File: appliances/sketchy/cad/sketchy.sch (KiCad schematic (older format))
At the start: 6 parts, among them J1 Barrel_Jack, M1 Stepper_Motor_bipolar, M2 Stepper_Motor_bipolar, U1 ESP32PICO-KIT

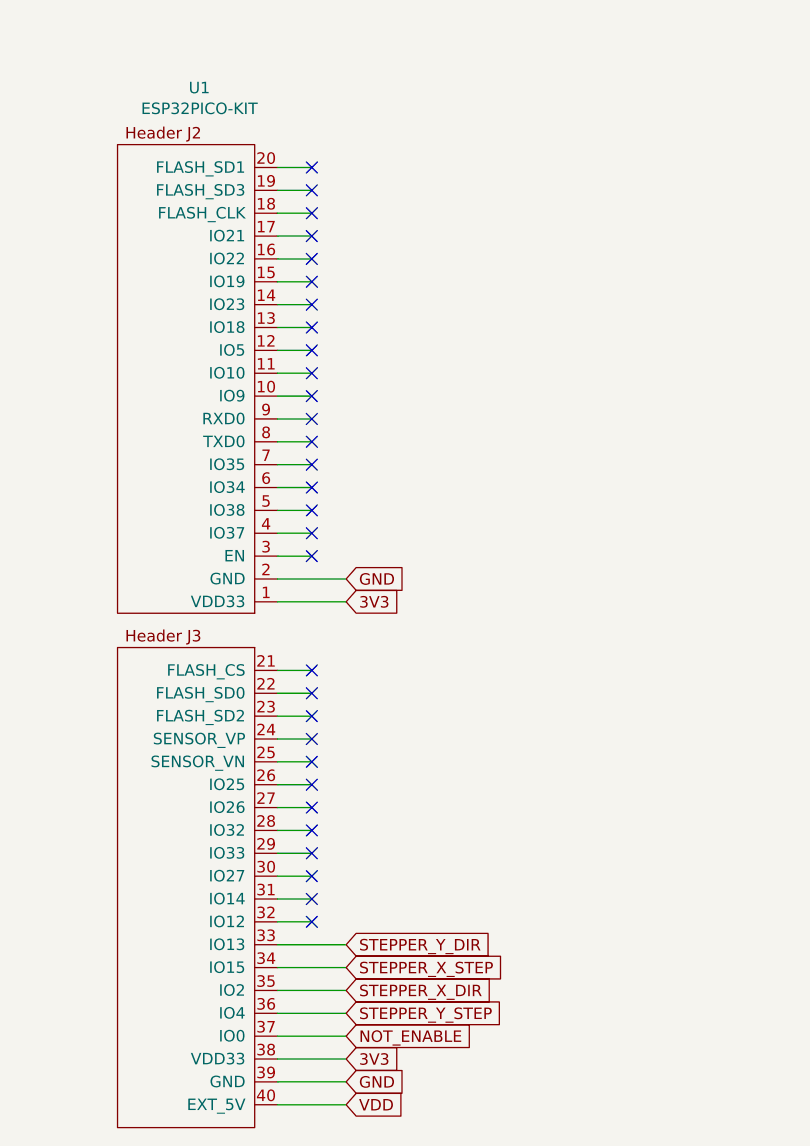
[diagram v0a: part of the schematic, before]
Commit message: Created smaller, square PCB with easy access to ESP32-PICO-KIT USB port.
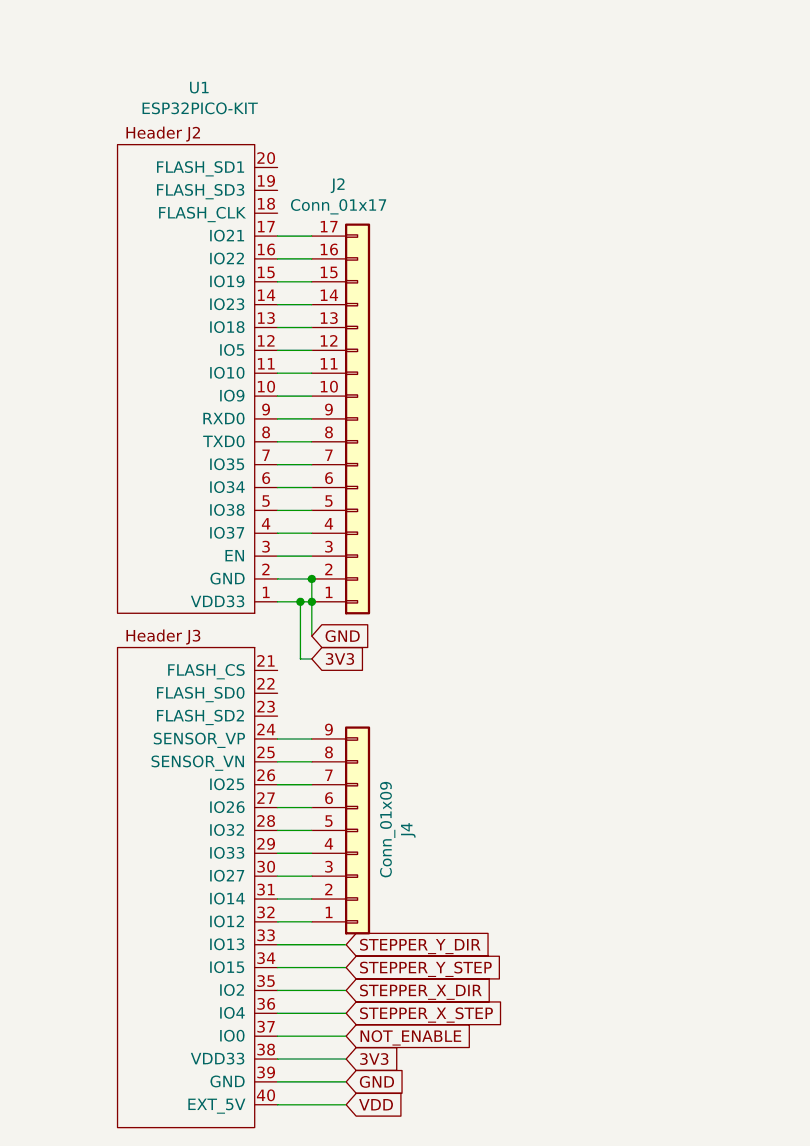
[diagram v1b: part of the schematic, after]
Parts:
- added J2: Conn_01x17, symbol Connector_Generic:Conn_01x17
- added J4: Conn_01x09, Pin_Header_Straight_1x09_Pitch2.54mm, symbol Connector_Generic:Conn_01x09
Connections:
- net GND is gone; now on net 3V3: A1.1 (GND), A1.10 (MS1), A1.11 (MS2), A1.12 (MS3), A1.7 (GND), A2.1 (GND), A2.10 (MS1), A2.11 (MS2), A2.12 (MS3), A2.7 (GND), J1.2, U1.2 (GND), U1.39 (GND)
- net 3V3: now also J2.1 (Pin_1), J2.2 (Pin_2)
- net STEPPER_X_STEP: now also U1.36 (IO4); no longer U1.34 (IO15)
- net STEPPER_Y_STEP: now also U1.34 (IO15); no longer U1.36 (IO4)
- net at U1.10 (IO9): now also J2.10 (Pin_10)
- net at U1.11 (IO10): now also J2.11 (Pin_11)
- net at U1.12 (IO5): now also J2.12 (Pin_12)
- net at U1.13 (IO18): now also J2.13 (Pin_13)
- net at U1.14 (IO23): now also J2.14 (Pin_14)
- net at U1.15 (IO19): now also J2.15 (Pin_15)
- net at U1.16 (IO22): now also J2.16 (Pin_16)
- net at U1.17 (IO21): now also J2.17 (Pin_17)
- net at U1.24 (SENSOR_VP): now also J4.9 (Pin_9)
- net at U1.25 (SENSOR_VN): now also J4.8 (Pin_8)
- net at U1.26 (IO25): now also J4.7 (Pin_7)
- net at U1.27 (IO26): now also J4.6 (Pin_6)
- net at U1.28 (IO32): now also J4.5 (Pin_5)
- net at U1.29 (IO33): now also J4.4 (Pin_4)
- net at U1.3 (EN): now also J2.3 (Pin_3)
- net at U1.30 (IO27): now also J4.3 (Pin_3)
- net at U1.31 (IO14): now also J4.2 (Pin_2)
- net at U1.32 (IO12): now also J4.1 (Pin_1)
- net at U1.4 (IO37): now also J2.4 (Pin_4)
- net at U1.5 (IO38): now also J2.5 (Pin_5)
- net at U1.6 (IO34): now also J2.6 (Pin_6)
- net at U1.7 (IO35): now also J2.7 (Pin_7)
- net at U1.8 (TXD0): now also J2.8 (Pin_8)
- net at U1.9 (RXD0): now also J2.9 (Pin_9)
- no-connect marks 30 -> 0
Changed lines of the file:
@@
 Text GLabel 3500 6100 2    50   Input ~ 0
 NOT_ENABLE
-Wire Wire Line
-	3500 4100 3200 4100
-Text GLabel 3500 4100 2    50   Input ~ 0
+Text GLabel 3350 4350 2    50   Input ~ 0
 GND
 Text GLabel 3500 6300 2    50   Input ~ 0
@@
 Wire Wire Line
 	3500 6300 3200 6300
-Text GLabel 3500 5800 2    50   Input ~ 0
+Text GLabel 3500 6000 2    50   Input ~ 0
 STEPPER_X_STEP
-Wire Wire Line
-	3500 5800 3200 5800
 Text GLabel 3500 5900 2    50   Input ~ 0
 STEPPER_X_DIR
@@
 Text GLabel 3500 5700 2    50   Input ~ 0
 STEPPER_Y_DIR
-Text GLabel 3500 6000 2    50   Input ~ 0
+Text GLabel 3500 5800 2    50   Input ~ 0
 STEPPER_Y_STEP
-Wire Wire Line
-	3500 6000 3200 6000
-Text GLabel 3500 4200 2    50   Input ~ 0
+Text GLabel 3350 4450 2    50   Input ~ 0
 3V3
-Wire Wire Line
-	3500 4200 3200 4200
 Text GLabel 3500 6200 2    50   Input ~ 0
 3V3
 Wire Wire Line
 	3500 6200 3200 6200
-NoConn ~ 3350 2300
-Wire Wire Line
-	3350 2300 3200 2300
-Wire Wire Line
-	3350 2400 3200 2400
-NoConn ~ 3350 2400
-Wire Wire Line
-	3350 2500 3200 2500
-NoConn ~ 3350 2500
-Wire Wire Line
-	3350 2600 3200 2600
-NoConn ~ 3350 2600
-Wire Wire Line
-	3350 2700 3200 2700
-NoConn ~ 3350 2700
-Wire Wire Line
-	3350 2800 3200 2800
-NoConn ~ 3350 2800
-Wire Wire Line
-	3350 2900 3200 2900
-NoConn ~ 3350 2900
-Wire Wire Line
-	3350 3000 3200 3000
-NoConn ~ 3350 3000
-Wire Wire Line
-	3350 3100 3200 3100
-NoConn ~ 3350 3100
-Wire Wire Line
-	3350 3200 3200 3200
-NoConn ~ 3350 3200
-Wire Wire Line
-	3350 3300 3200 3300
-NoConn ~ 3350 3300
-Wire Wire Line
-	3350 3400 3200 3400
-NoConn ~ 3350 3400
-Wire Wire Line
-	3350 3500 3200 3500
-NoConn ~ 3350 3500
-Wire Wire Line
-	3350 3600 3200 3600
-NoConn ~ 3350 3600
-Wire Wire Line
-	3350 3700 3200 3700
-NoConn ~ 3350 3700
-Wire Wire Line
-	3350 3800 3200 3800
-NoConn ~ 3350 3800
-Wire Wire Line
-	3350 3900 3200 3900
-NoConn ~ 3350 3900
-Wire Wire Line
-	3350 4000 3200 4000
-NoConn ~ 3350 4000
-Wire Wire Line
-	3350 4500 3200 4500
-NoConn ~ 3350 4500
-Wire Wire Line
-	3350 4600 3200 4600
-NoConn ~ 3350 4600
-Wire Wire Line
-	3350 4700 3200 4700
-NoConn ~ 3350 4700
-Wire Wire Line
-	3350 4800 3200 4800
-NoConn ~ 3350 4800
-Wire Wire Line
-	3350 4900 3200 4900
-NoConn ~ 3350 4900
-Wire Wire Line
-	3350 5000 3200 5000
-NoConn ~ 3350 5000
-Wire Wire Line
-	3350 5100 3200 5100
-NoConn ~ 3350 5100
-Wire Wire Line
-	3350 5200 3200 5200
-NoConn ~ 3350 5200
-Wire Wire Line
-	3350 5300 3200 5300
-NoConn ~ 3350 5300
-Wire Wire Line
-	3350 5400 3200 5400
-NoConn ~ 3350 5400
-Wire Wire Line
-	3350 5500 3200 5500
-NoConn ~ 3350 5500
-Wire Wire Line
-	3350 5600 3200 5600
-NoConn ~ 3350 5600
 Wire Wire Line
 	7100 4550 7250 4550
@@
 Wire Wire Line
 	3500 5700 3200 5700
+Wire Wire Line
+	3500 5800 3200 5800
+Wire Wire Line
+	3500 6000 3200 6000
+$Comp
+L Connector_Generic:Conn_01x09 J4
+U 1 1 5DDFE4C5
+P 3550 5200
+F 0 "J4" V 3767 5196 50  0000 C CNN
+F 1 "Conn_01x09" V 3676 5196 50  0000 C CNN
+F 2 "Pin_Header_Straight_1x09_Pitch2.54mm" H 3550 5200 50  0001 C CNN
+F 3 "~" H 3550 5200 50  0001 C CNN
+	1    3550 5200
+	1    0    0    1
+$EndComp
+Wire Wire Line
+	3200 5600 3350 5600
+Wire Wire Line
+	3350 5500 3200 5500
+Wire Wire Line
+	3200 5400 3350 5400
+Wire Wire Line
+	3350 5300 3200 5300
+Wire Wire Line
+	3200 5200 3350 5200
+Wire Wire Line
+	3350 5100 3200 5100
+Wire Wire Line
+	3200 5000 3350 5000
+Wire Wire Line
+	3350 4900 3200 4900
+Wire Wire Line
+	3200 4800 3350 4800
+$Comp
+L Connector_Generic:Conn_01x17 J2
+U 1 1 5DDFE417
+P 3550 3400
+F 0 "J2" H 3468 2375 50  0000 C CNN
+F 1 "Conn_01x17" H 3468 2466 50  0000 C CNN
+F 2 "" H 3550 3400 50  0001 C CNN
+F 3 "~" H 3550 3400 50  0001 C CNN
+	1    3550 3400
+	1    0    0    1
+$EndComp
+Wire Wire Line
+	3350 4100 3200 4100
+Wire Wire Line
+	3350 4200 3300 4200
+Wire Wire Line
+	3350 4000 3200 4000
+Wire Wire Line
+	3350 3900 3200 3900
+Wire Wire Line
+	3200 3800 3350 3800
+Wire Wire Line
+	3350 3700 3200 3700
+Wire Wire Line
+	3200 3600 3350 3600
+Wire Wire Line
+	3350 3500 3200 3500
+Wire Wire Line
+	3200 3400 3350 3400
+Wire Wire Line
+	3350 3300 3200 3300
+Wire Wire Line
+	3200 3200 3350 3200
+Wire Wire Line
+	3350 3100 3200 3100
+Wire Wire Line
+	3200 3000 3350 3000
+Wire Wire Line
+	3350 2900 3200 2900
+Wire Wire Line
+	3200 2800 3350 2800
+Wire Wire Line
+	3350 2700 3200 2700
+Wire Wire Line
+	3200 2600 3350 2600
+Connection ~ 3350 4100
+Wire Wire Line
+	3350 4100 3350 4200
+Wire Wire Line
+	3350 4450 3300 4450
+Wire Wire Line
+	3300 4450 3300 4200
+Connection ~ 3300 4200
+Wire Wire Line
+	3300 4200 3200 4200
+Connection ~ 3350 4200
+Wire Wire Line
+	3350 4200 3350 4350
 $EndSCHEMATC

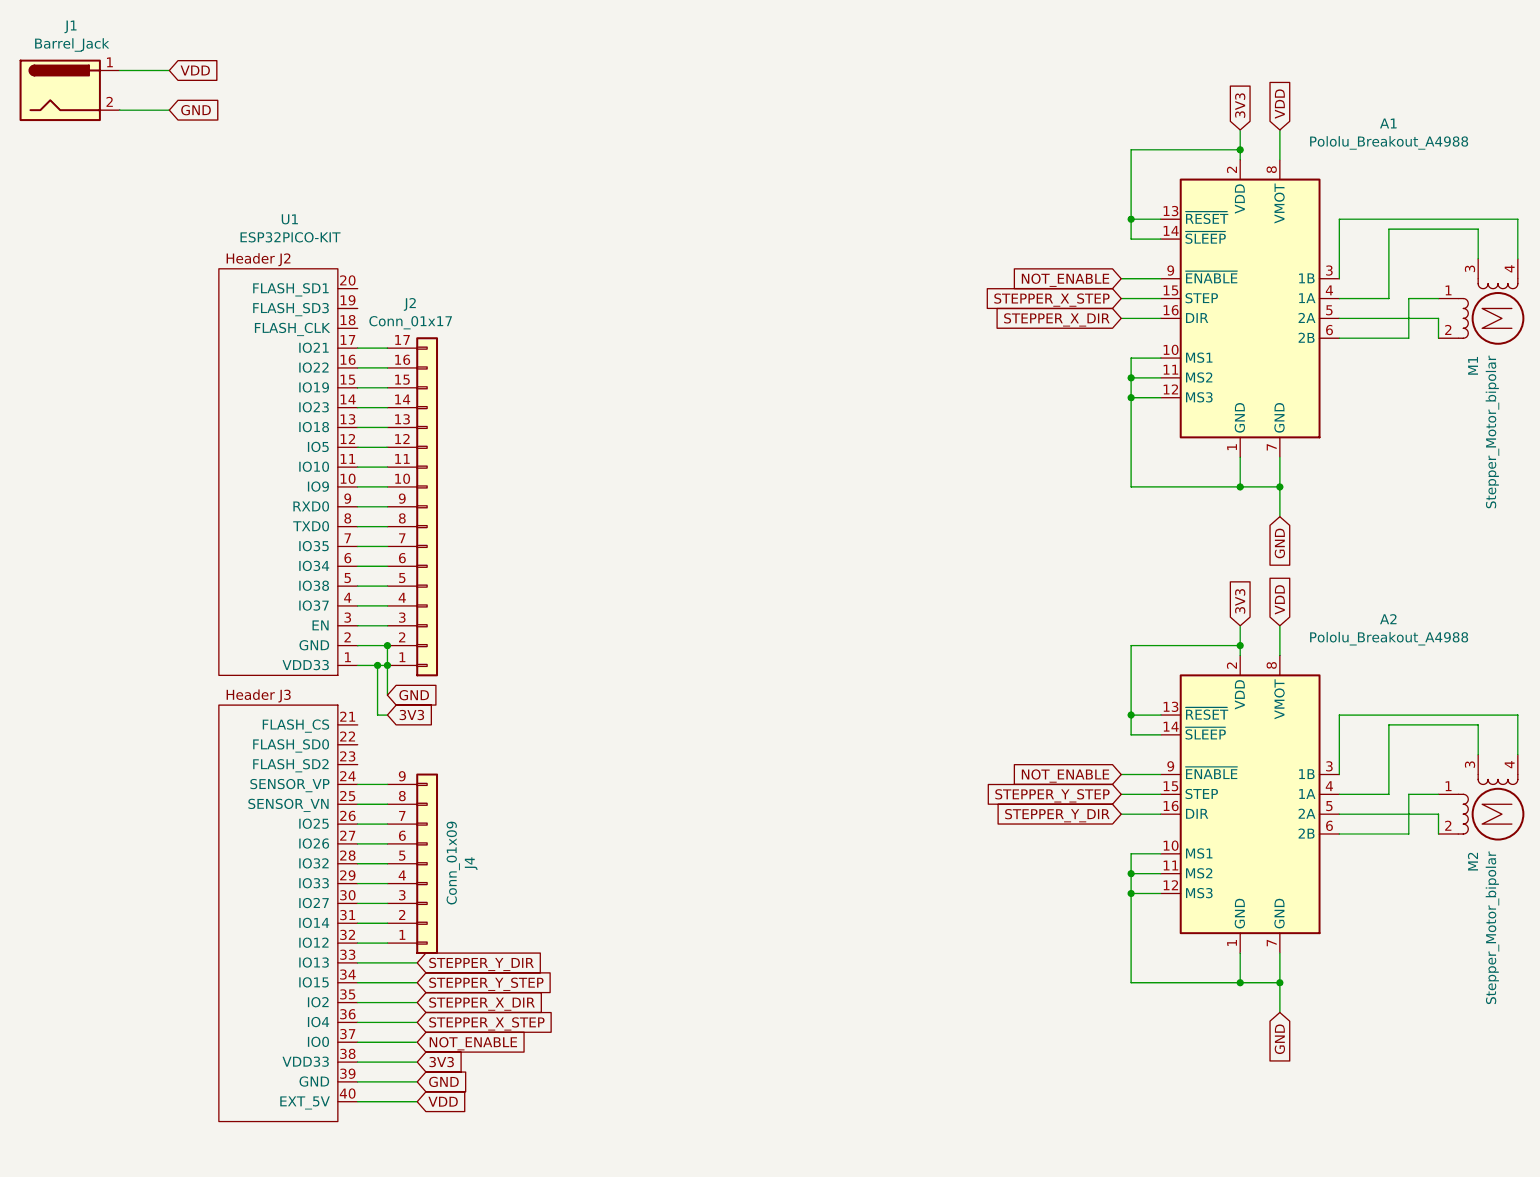
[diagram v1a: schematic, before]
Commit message: Removed rogue schematic connection between GND and 3V3 at ESP32-PICO-KIT pin 1 / header junction. Luckily, it doesn't appear as though that connection was ever propagated to the PCB.
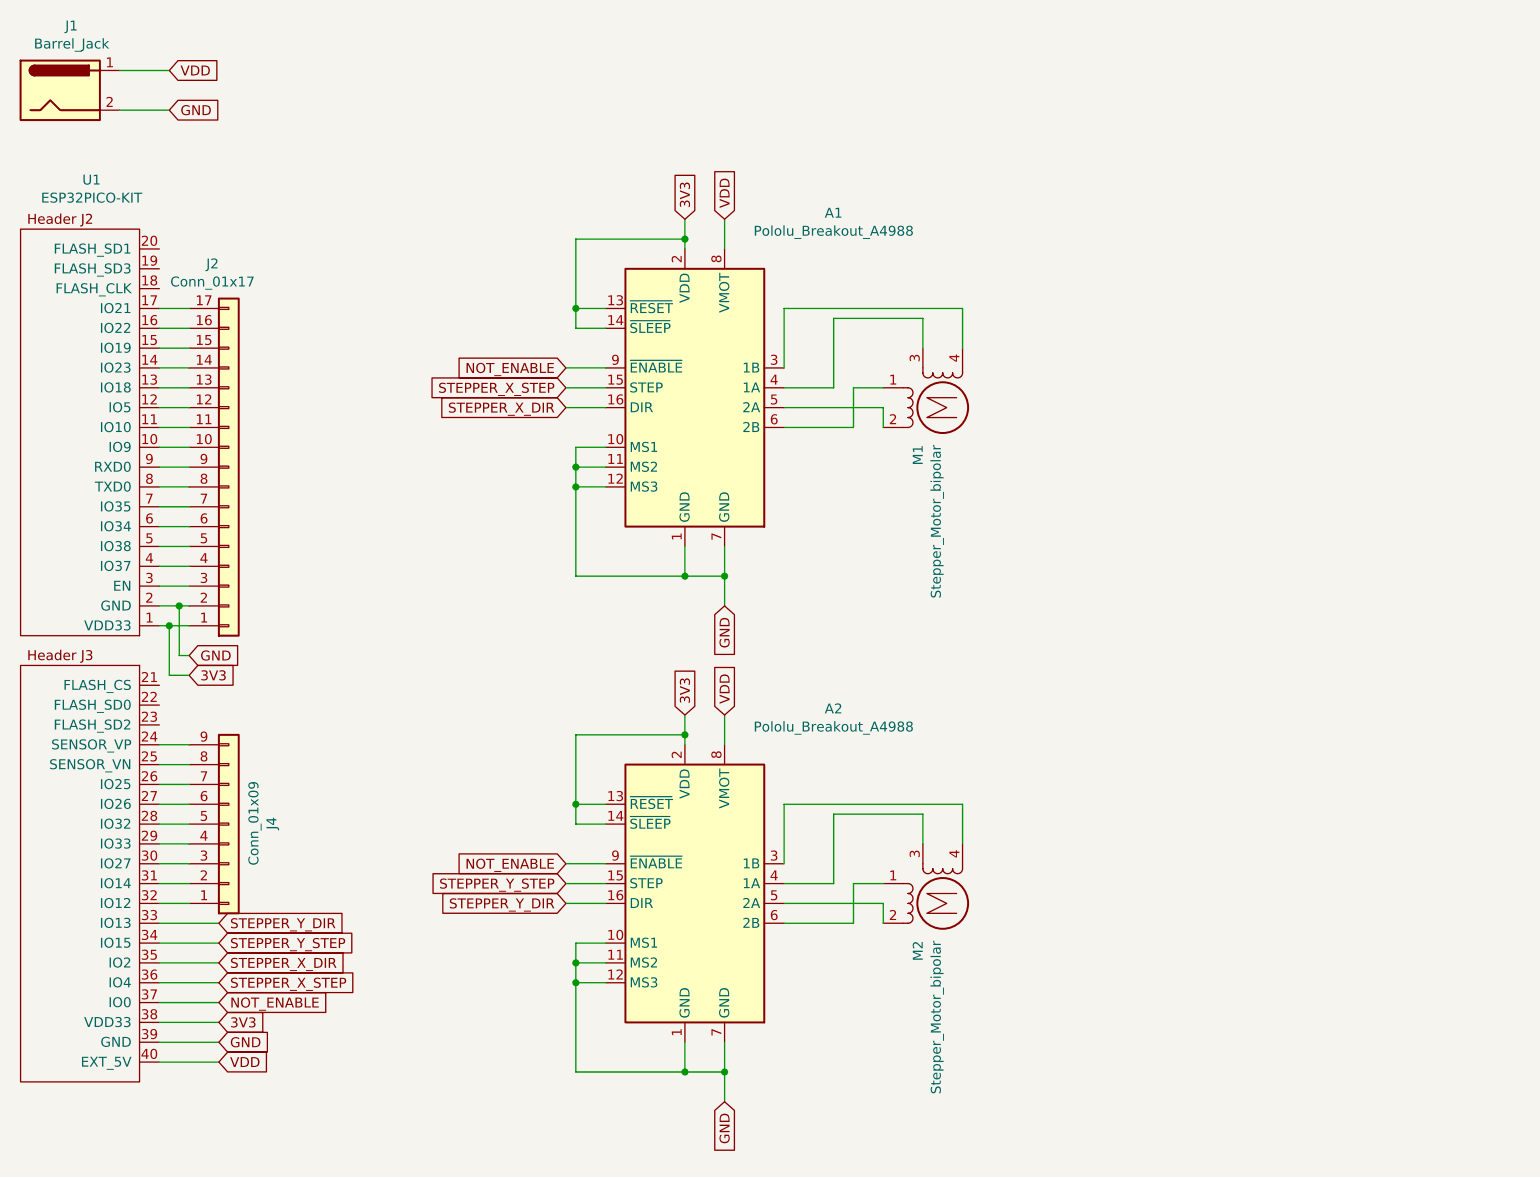
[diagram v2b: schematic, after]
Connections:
- net 3V3: no longer A1.1 (GND), A1.10 (MS1), A1.11 (MS2), A1.12 (MS3), A1.7 (GND), A2.1 (GND), A2.10 (MS1), A2.11 (MS2), A2.12 (MS3), A2.7 (GND), J1.2, J2.2 (Pin_2), U1.2 (GND), U1.39 (GND)
- new net GND: A1.1 (GND), A1.10 (MS1), A1.11 (MS2), A1.12 (MS3), A1.7 (GND), A2.1 (GND), A2.10 (MS1), A2.11 (MS2), A2.12 (MS3), A2.7 (GND), J1.2, J2.2 (Pin_2), U1.2 (GND), U1.39 (GND)
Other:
- moved on the sheet: A1, A2, J2, J4, M1, M2, U1
